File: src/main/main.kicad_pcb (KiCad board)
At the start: 4 copper layers, 170 x 170 mm, 45 parts, among them J101 Conn_02x05_Odd_Even, J201 Conn_01x06, J202 Conn_01x10, J301 Conn_02x12_Top_Bottom, J302 Conn_01x12, J401 Conn_02x05_Odd_Even, J501 Conn_01x03, J601 Conn_01x03, J701 Conn_01x03, P101 SMTSO3035CTJ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

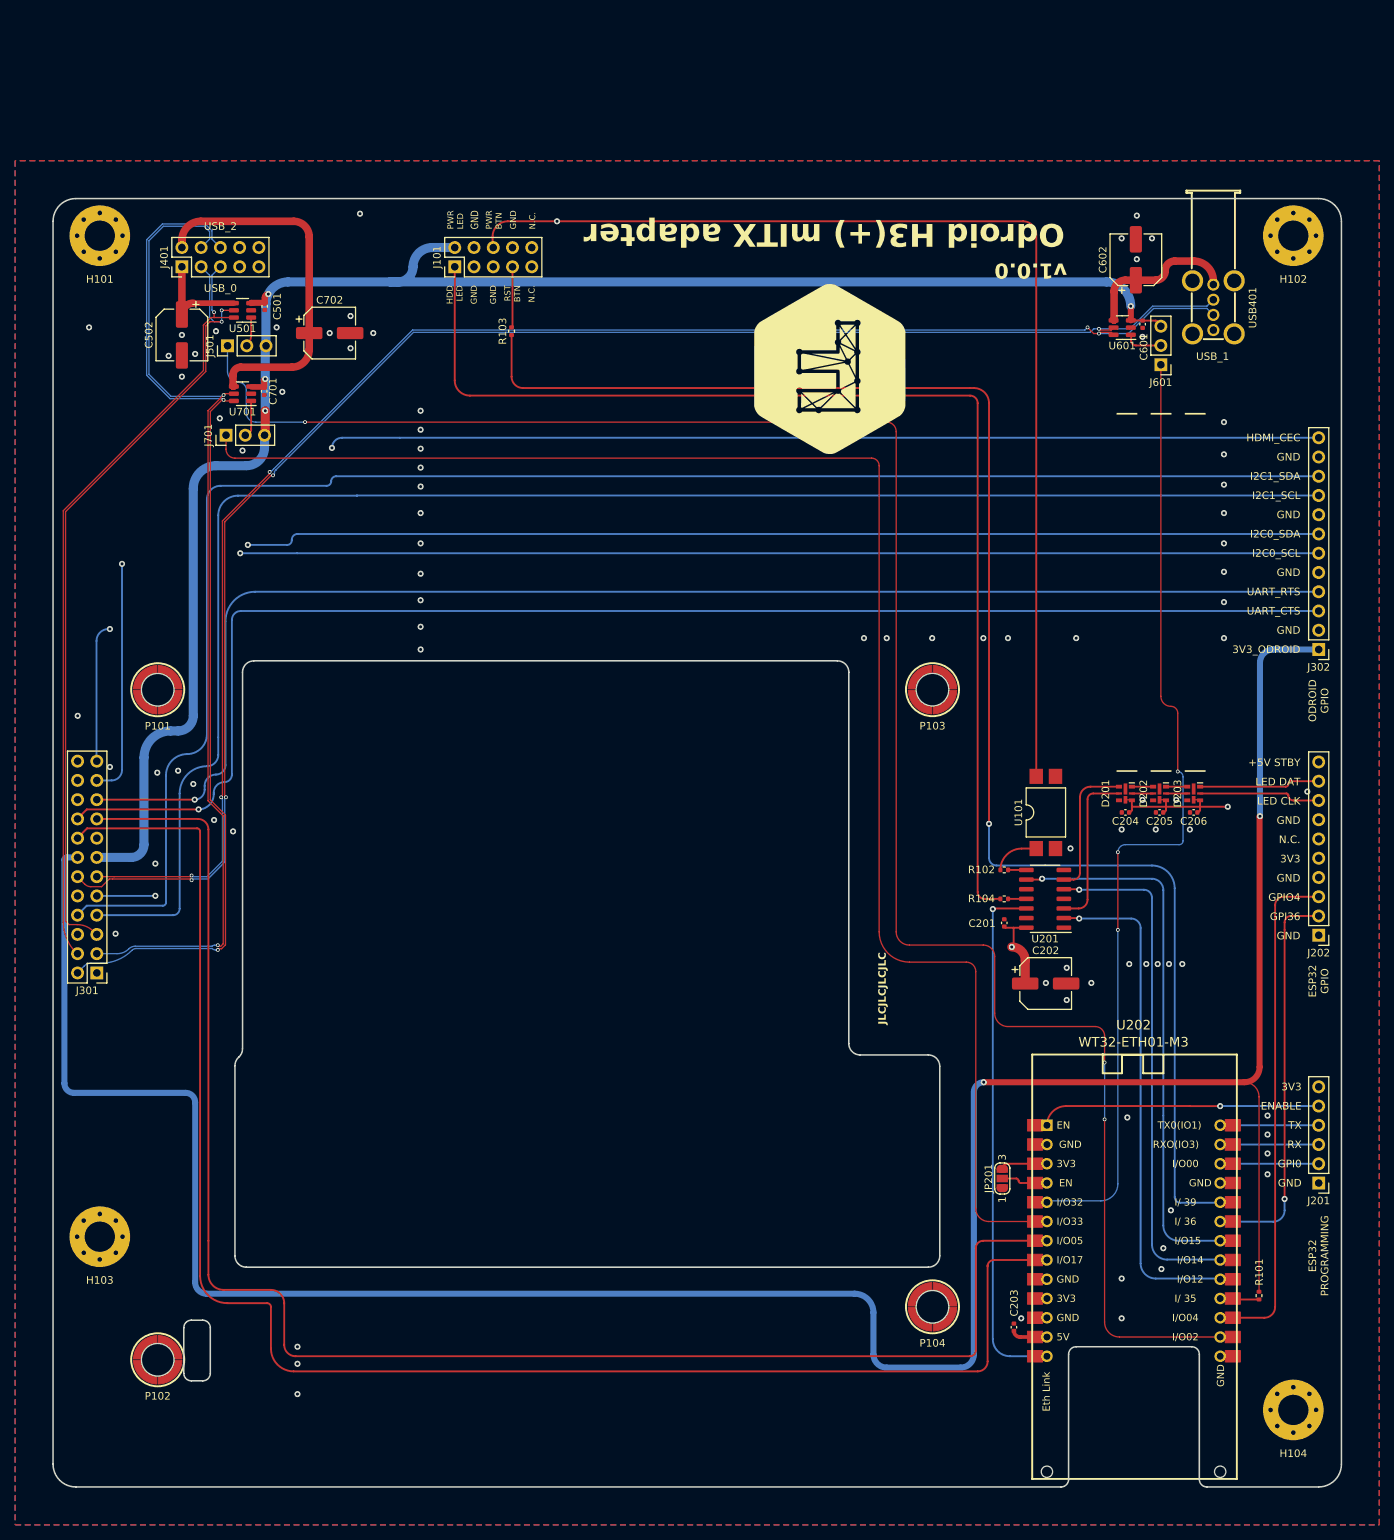
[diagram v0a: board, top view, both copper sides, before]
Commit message: Fix wrong header pinout
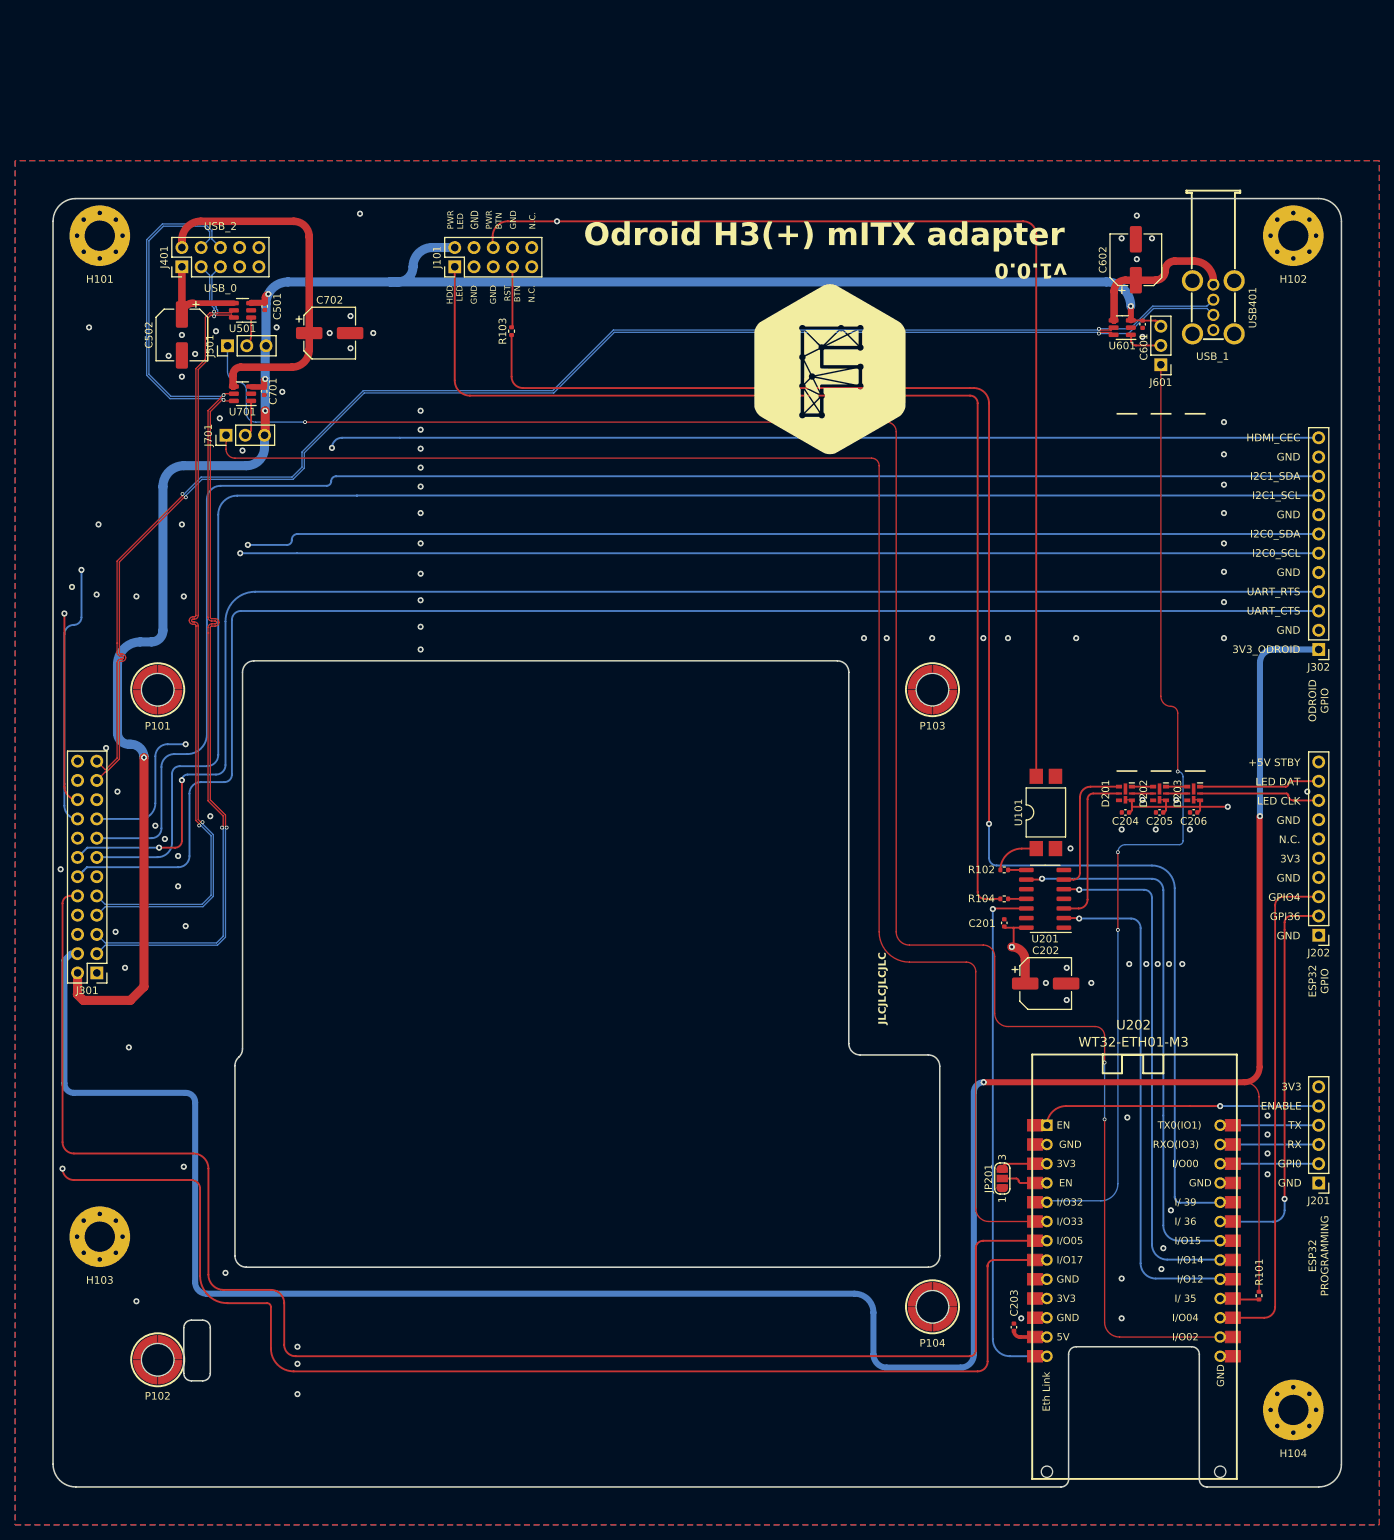
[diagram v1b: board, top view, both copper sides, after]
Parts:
- J301: value Conn_02x12_Top_Bottom -> Conn_02x12_Odd_Even
- turned G*** to 0 degrees
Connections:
- J301 pad 10: GND -> /Odroid H3+/UART0_TX
- J301 pad 11: /USB/USB1_DP -> GND
- J301 pad 12: /USB/USB1_DN -> /Odroid H3+/UART0_CTS
- J301 pad 13: /+5V_RUN -> /Odroid H3+/I2C1_SCL
- J301 pad 14: /Odroid H3+/+3V3_RUN -> /Odroid H3+/UART0_RTS
- J301 pad 15: GND -> /Odroid H3+/12C1_SDA
- J301 pad 16: /Odroid H3+/UART0_RX -> GND
- J301 pad 17: /Odroid H3+/UART0_TX -> /PWR_BTN
- J301 pad 18: /Odroid H3+/UART0_CTS -> /Odroid H3+/I2C0_SCL
- J301 pad 19: /Odroid H3+/UART0_RTS -> GND
- J301 pad 2: /USB/USB2_DP -> /+5V_RUN
- J301 pad 20: GND -> /Odroid H3+/12C0_SDA
- J301 pad 21: /Odroid H3+/I2C0_SCL -> /USB/USB1_DP
- J301 pad 22: /Odroid H3+/12C0_SDA -> /Odroid H3+/HDMI_CEC
- J301 pad 23: /Odroid H3+/HDMI_CEC -> /USB/USB1_DN
- J301 pad 3: /USB/USB2_DN -> /USB/USB2_DP
- J301 pad 4: /USB/USB0_DP -> /Odroid H3+/+3V3_RUN
- J301 pad 5: /USB/USB0_DN -> /USB/USB2_DN
- J301 pad 7: /Odroid H3+/I2C1_SCL -> /USB/USB0_DP
- J301 pad 8: /Odroid H3+/12C1_SDA -> /Odroid H3+/UART0_RX
- J301 pad 9: /PWR_BTN -> /USB/USB0_DN
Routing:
- net /+5V_RUN: track 230.2 -> 260.7 mm, vias 4 -> 5
- net /USB/USB1_DN: track 211.4 -> 193.2 mm, vias 4 -> 2
- net /USB/USB1_DP: track 208.3 -> 193.3 mm, vias 5 -> 2
- net /Odroid H3+/+3V3_RUN: track 350.9 -> 337.9 mm
- net /Odroid H3+/12C1_SDA: track 216.8 -> 204.9 mm
- net /PWR_BTN: track 292.8 -> 282.7 mm
- net /Odroid H3+/I2C0_SCL: track 189.9 -> 199.9 mm
- net /Odroid H3+/UART0_RTS: track 185.0 -> 194.9 mm, vias 1 -> 2
- net /Odroid H3+/UART0_RX: track 208.9 -> 199.3 mm, vias 0 -> 1
- net /Odroid H3+/HDMI_CEC: track 201.9 -> 210.8 mm, vias 2 -> 1
- net /Odroid H3+/UART0_CTS: track 187.9 -> 195.7 mm, vias 1 -> 0
- net /Odroid H3+/I2C1_SCL: track 212.6 -> 205.7 mm
- net /Odroid H3+/UART0_TX: track 206.0 -> 200.9 mm
- net /USB/USB0_DP: track 102.9 -> 106.7 mm, vias 1 -> 2
- net /USB/USB2_DP: track 137.7 -> 135.5 mm
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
